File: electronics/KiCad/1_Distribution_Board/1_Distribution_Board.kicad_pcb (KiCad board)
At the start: 2 copper layers, 130 x 120 mm, 135 parts, among them J1 Jumper Pins, J10 Conn_01x08_Socket, J11 Conn_01x08_Socket, J12 Conn_01x02, J13 Conn_01x02, J14 Conn_01x08_Socket, J15 Conn_01x08_Socket, J16 JST VH, J17 JST VH, J18 JST VH, J2 Jumper Pins, J20 Conn_01x04, J24 Generic 2.54mm, J25 Generic 2.54mm, J26 Generic 2.54mm, J27 Generic 2.54mm, J28 Generic 2.54mm, J29 Generic 2.54mm, J3 JST PH, J32 Jumper Pins, J33 Jumper Pins, J34 JST PH, J35 Generic 2.54mm, J36 Conn_01x08_Socket, J37 Conn_01x02_Socket, J38 Conn_01x08_Socket, J39 Jumper Pins, J4 Generic 2.54mm, J40 Jumper Pins, J41 JST PH, J42 Generic 2.54mm, J43 Conn_01x08_Socket, J44 Conn_01x02_Socket, J45 Conn_01x08_Socket, J46 Jumper Pins, J47 Jumper Pins, J48 JST PH, J49 Generic 2.54mm, J5 Conn_01x08_Socket, J50 Conn_01x08_Socket, J51 Conn_01x02_Socket, J52 Conn_01x08_Socket, J53 Conn_01x10, J54 Conn_01x06, J55 Signals 0-3, J56 Signals 4-7, J57 Module Left, J58 Conn_02x08_Odd_Even, J59 Module Right, J6 Conn_01x02_Socket, J60 Signals 8-11, J61 Signals 12-15, J7 Conn_01x08_Socket, J8 Conn_01x02, J9 Conn_01x02, M1 MountingHole_3.2mm_M3_ISO7380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, Q1 DMG2305UX, Q2 BS170, Q3 BS170, SW1 SW_Push, U1 R-786.5-0.5, U2 R-78B12-2.0, U3 R-78C5.0-1.0

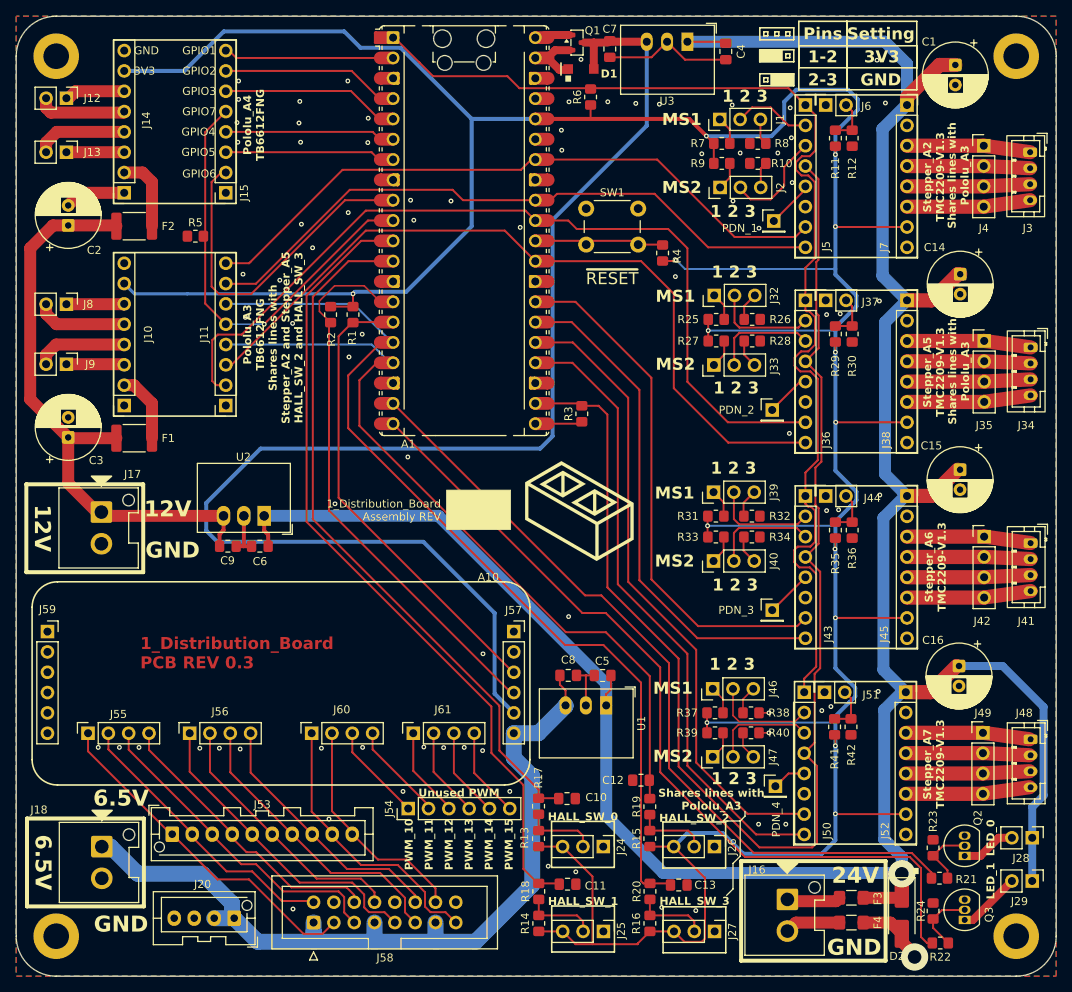
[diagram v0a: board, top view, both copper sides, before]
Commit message: Merge board v1.3 into main (clean-clone fixups, generated files trimmed to main level) (#289)
* Initial start to updates

Removed motor pages, updated Q2,Q3, Cleaned up power module connections.

- Still need to correct routing for these updates.

* PCA Update

Updated PCA to have level shifter for I2C lines and external oscillator for precision. Corrected Power to pull from 12V.

* Removed old circuits from PCB

Removed all unused traces

* Mid work update

Lots of rework on the SCH and PCB. Checkpoint.

* Updated with more layout

Compelted PCA on board.

* adding libraries

* REV0.9 for review

Took care of all open items on the electronics PCB except for the driver resistor addresses.

* Updates Just prior to Ordering V1.0 PCBs

Updates Just prior to Ordering V1.0 PCBs

* Updates to push to V1.0

Updates to push to V1.0

* Updates to push to V1.0 missing saves. . .

Updates to push to V1.0 missing saves. . .

* Correcting Part rotation for JLCPCB

Several parts needed the "FT Rotation Offset" parameter added to correct for part orientation for JLCPCB order.

* All orientations corrected

* latest update

* Updated to reflect V1.0 of layer board as well

Updated for initial orders with PCA module populated. Also updated to layer boards for flex cables.

* Updated data and notes

* Corrected SCH for power sequence issue

5V to Vsys for all powered items.
Correction of the PCA9306 power pins.
Added decoupling to oscillator and PCA9306.

* Updated for changes to the SCH items

Updated PCB to include all changed from the SCH.

* Updated rules to correct errors

Cleaned up rules a bit to prevent false errors.

* Started work on silk update

Slowly started work on silk update.

* Corrected the 10k to 1k for connecting resistors

R1 got fixed for the correct 1k instead of 10k for UART1

* Updated Silk on PCB

Added notes for describing the pins better in the silk layer.

* Updated REV to 1.3 to reflect changes

* Updated with Version 1.3

* KiCad: make the v1.3 project 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
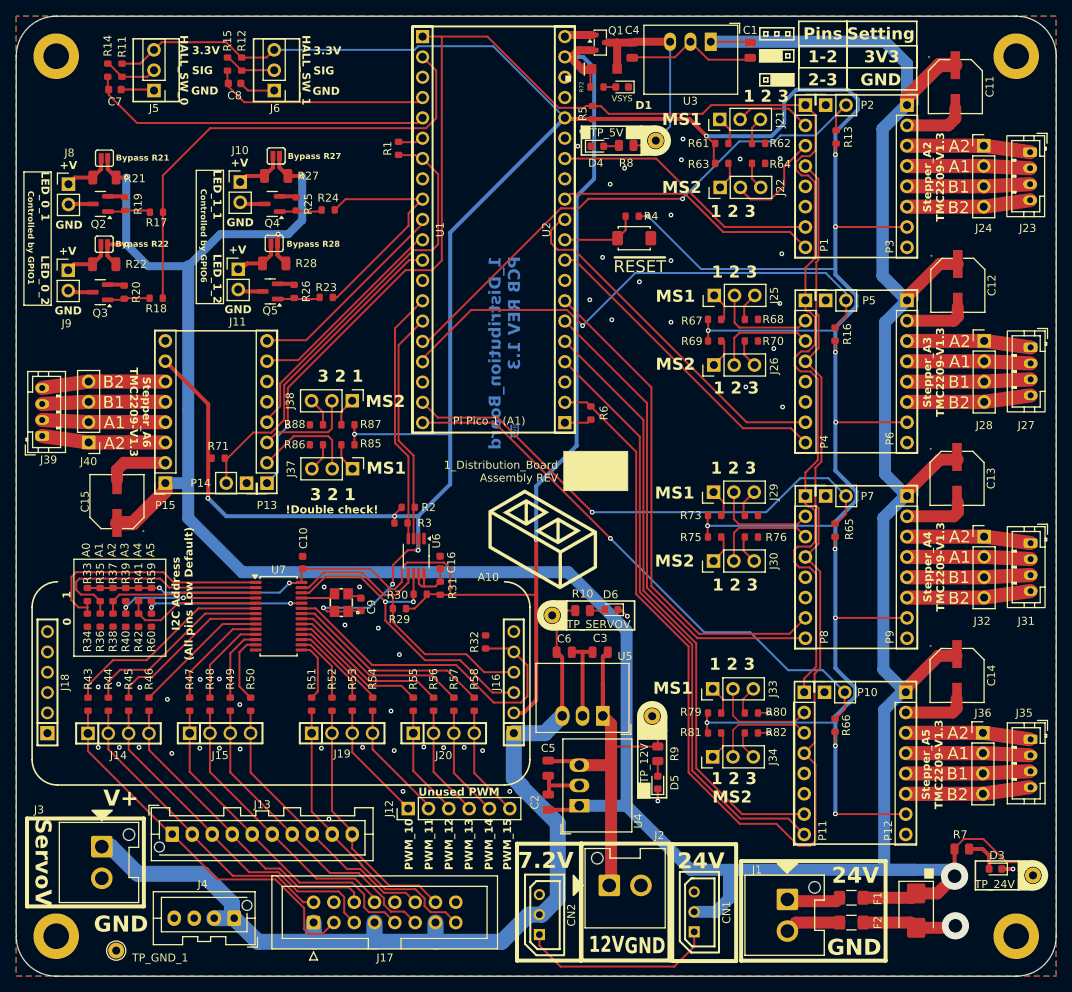
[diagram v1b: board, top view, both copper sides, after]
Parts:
- removed A1: Raspberry Pi Pico 1, Module:RaspberryPi_Pico_Common_Unspecified
- removed the C11 at (93.9, 133.5)
- removed the C12 at (103.1, 120.5)
- removed the C13 at (107.8, 133.6)
- removed the F1 at (39.8, 77.8)
- removed the F2 at (39.8, 51.2)
- removed the J12 at (31.3, 35.2)
- removed the J13 at (31.3, 42.0)
- removed the J26 at (112.3, 128.8)
- removed the J27 at (112.3, 139.4)
- removed the J36 at (123.7, 60.5)
- removed J43, J45, J50, J52, J7: Conn_01x08_Socket, Connector_PinSocket_2.54mm:PinSocket_1x08_P2.54mm_Vertical
- removed J44, J51: Conn_01x02_Socket, Connector_PinSocket_2.54mm:PinSocket_1x02_P2.54mm_Vertical
- removed the J5 at (123.7, 36.1)
- removed J55: Signals 0-3, Connector_PinSocket_2.54mm:PinSocket_1x04_P2.54mm_Vertical
- removed J56: Signals 4-7, Connector_PinSocket_2.54mm:PinSocket_1x04_P2.54mm_Vertical
- removed J57: Module Left, Connector_PinSocket_2.54mm:PinSocket_1x06_P2.54mm_Vertical
- removed J59: Module Right, Connector_PinSocket_2.54mm:PinSocket_1x06_P2.54mm_Vertical
- removed the J6 at (126.2, 36.1)
- removed J60: Signals 8-11, Connector_PinSocket_2.54mm:PinSocket_1x04_P2.54mm_Vertical
- removed J61: Signals 12-15, Connector_PinSocket_2.54mm:PinSocket_1x04_P2.54mm_Vertical
- removed the J8 at (31.3, 61.0)
- removed the J9 at (31.3, 68.5)
- removed PDN_1, PDN_2, PDN_3, PDN_4: PTH, Connector_PinHeader_2.54mm:PinHeader_1x01_P2.54mm_Vertical
- removed SW1: SW_Push, Button_Switch_THT:SW_PUSH_6mm
- added C1: 10uF, PCM_JLCPCB:C_0805, F.Cu at (116.8, 29.2)
- added C15: 100uF, EasyEDA:CAP-SMD_BD6.3-L6.6-W6.6-LS7.4-FD, F.Cu at (37.6, 85.7)
- added C16: 100nF, PCM_JLCPCB:C_0603, F.Cu at (78.0, 93.3)
- added CN1: HC-5264-3A, EasyEDA:CONN-TH_3P-P2.50_HCTL_HC-5264-3A, F.Cu at (109.8, 137.0)
- added CN2: HC-5264-3A, EasyEDA:CONN-TH_3P-P2.50_HCTL_HC-5264-3A, F.Cu at (90.4, 137.3)
- added D3: Yellow, PCM_JLCPCB:D_0603, F.Cu at (147.4, 131.6)
- added D4: Yellow, PCM_JLCPCB:D_0603, F.Cu at (97.7, 41.2)
- added D5: Yellow, PCM_JLCPCB:D_0603, F.Cu at (105.2, 120.8)
- added D6: Yellow, PCM_JLCPCB:D_0603, F.Cu at (99.4, 99.2)
- added D7: Yellow, PCM_JLCPCB:D_0603, F.Cu at (100.7, 33.8)
- added J16: PM254V-11-06-H85, EasyEDA:HDR-TH_6P-P2.54-V-F, F.Cu at (87.2, 108.3)
- added J18: PM254V-11-06-H85, EasyEDA:HDR-TH_6P-P2.54-V-F, F.Cu at (28.9, 108.3)
- added J19: 2.54-1*4P母, EasyEDA:HDR-TH_4P-P2.54-V-F, F.Cu at (65.7, 114.6)
- added J20: 2.54-1*4P母, EasyEDA:HDR-TH_4P-P2.54-V-F, F.Cu at (78.4, 114.6)
- added J39: JST PH, Connector_JST:JST_PH_B4B-PH-K_1x04_P2.00mm_Vertical, F.Cu at (28.3, 77.5)
- added J40: Generic 2.54mm, Connector_PinHeader_2.54mm:PinHeader_1x04_P2.54mm_Vertical, F.Cu at (34.1, 78.3)
- added JAW: Maker's Mark, JAW:JAW, B.Cu at (87.4, 76.8)
- added JP1: ~, PCM_SparkFun-Jumper:Jumper_2_NO, F.Cu at (36.0, 42.8)
- added JP2: ~, PCM_SparkFun-Jumper:Jumper_2_NO, F.Cu at (36.0, 53.5)
- added JP3: ~, PCM_SparkFun-Jumper:Jumper_2_NO, F.Cu at (57.5, 42.5)
- added JP4: ~, PCM_SparkFun-Jumper:Jumper_2_NO, F.Cu at (57.2, 53.4)
- added P1: Header-Female-2.54_1x8, Connector_PinSocket_2.54mm:PinSocket_1x08_P2.54mm_Vertical, F.Cu at (123.7, 36.1)
- added P10: Header-Female-2.54_1x8, Connector_PinSocket_2.54mm:PinSocket_1x08_P2.54mm_Vertical, F.Cu at (123.5, 109.5)
- added P11: Header-Female-2.54_1x2, Connector_PinSocket_2.54mm:PinSocket_1x02_P2.54mm_Vertical, F.Cu at (126.0, 109.5)
- added P12: Header-Female-2.54_1x8, Connector_PinSocket_2.54mm:PinSocket_1x08_P2.54mm_Vertical, F.Cu at (136.2, 109.5)
- added P13: Header-Female-2.54_1x8, Connector_PinSocket_2.54mm:PinSocket_1x08_P2.54mm_Vertical, F.Cu at (56.3, 83.4)
- added P14: Header-Female-2.54_1x2, Connector_PinSocket_2.54mm:PinSocket_1x02_P2.54mm_Vertical, F.Cu at (53.8, 83.4)
- added P15: Header-Female-2.54_1x8, Connector_PinSocket_2.54mm:PinSocket_1x08_P2.54mm_Vertical, F.Cu at (43.6, 83.4)
- added P2: Header-Female-2.54_1x2, Connector_PinSocket_2.54mm:PinSocket_1x02_P2.54mm_Vertical, F.Cu at (126.2, 36.1)
- added P3: Header-Female-2.54_1x8, Connector_PinSocket_2.54mm:PinSocket_1x08_P2.54mm_Vertical, F.Cu at (136.3, 36.1)
- added P4: Header-Female-2.54_1x8, Connector_PinSocket_2.54mm:PinSocket_1x08_P2.54mm_Vertical, F.Cu at (123.7, 60.5)
- added P5: Header-Female-2.54_1x2, Connector_PinSocket_2.54mm:PinSocket_1x02_P2.54mm_Vertical, F.Cu at (126.2, 60.5)
- added P6: Header-Female-2.54_1x8, Connector_PinSocket_2.54mm:PinSocket_1x08_P2.54mm_Vertical, F.Cu at (136.3, 60.5)
- added P7: Header-Female-2.54_1x8, Connector_PinSocket_2.54mm:PinSocket_1x08_P2.54mm_Vertical, F.Cu at (123.7, 85.0)
- added P8: Header-Female-2.54_1x2, Connector_PinSocket_2.54mm:PinSocket_1x02_P2.54mm_Vertical, F.Cu at (126.2, 85.0)
- added P9: Header-Female-2.54_1x8, Connector_PinSocket_2.54mm:PinSocket_1x08_P2.54mm_Vertical, F.Cu at (136.3, 85.0)
- added Q4: AO3400A, PCM_JLCPCB:Q_SOT-23, F.Cu at (57.0, 48.5)
- added Q5: AO3400A, PCM_JLCPCB:Q_SOT-23, F.Cu at (56.8, 59.4)
- added R43: 220Ω, PCM_JLCPCB:R_0603, F.Cu at (34.0, 111.0)
- added R44: 220Ω, PCM_JLCPCB:R_0603, F.Cu at (36.5, 111.0)
- added R45: 220Ω, PCM_JLCPCB:R_0603, F.Cu at (39.1, 111.0)
- added R46: 220Ω, PCM_JLCPCB:R_0603, F.Cu at (41.6, 111.0)
- added R47: 220Ω, PCM_JLCPCB:R_0603, F.Cu at (46.7, 111.0)
- added R48: 220Ω, PCM_JLCPCB:R_0603, F.Cu at (49.2, 111.0)
- added R49: 220Ω, PCM_JLCPCB:R_0603, F.Cu at (51.8, 111.0)
- added R50: 220Ω, PCM_JLCPCB:R_0603, F.Cu at (54.3, 111.0)
- added R51: 220Ω, PCM_JLCPCB:R_0603, F.Cu at (61.9, 111.0)
- added R52: 220Ω, PCM_JLCPCB:R_0603, F.Cu at (64.5, 111.0)
- added R53: 220Ω, PCM_JLCPCB:R_0603, F.Cu at (67.0, 111.0)
- added R54: 220Ω, PCM_JLCPCB:R_0603, F.Cu at (69.6, 111.0)
- added R55: 220Ω, PCM_JLCPCB:R_0603, F.Cu at (74.6, 111.0)
- added R56: 220Ω, PCM_JLCPCB:R_0603, F.Cu at (77.2, 111.0)
- added R57: 220Ω, PCM_JLCPCB:R_0603, F.Cu at (79.7, 111.0)
- added R58: 220Ω, PCM_JLCPCB:R_0603, F.Cu at (82.3, 111.0)
- added R59: 10kΩ, PCM_JLCPCB:R_0603, F.Cu at (41.9, 97.3)
- added R60: 10kΩ, PCM_JLCPCB:R_0603, F.Cu at (41.9, 100.5)
- added R61: 10kΩ, PCM_JLCPCB:R_0603, F.Cu at (113.2, 40.9)
- added R62: 10kΩ, PCM_JLCPCB:R_0603, F.Cu at (117.8, 40.9)
- added R63: 10kΩ, PCM_JLCPCB:R_0603, F.Cu at (113.2, 43.4)
- added R64: 10kΩ, PCM_JLCPCB:R_0603, F.Cu at (117.8, 43.4)
- added R65: 10kΩ, PCM_JLCPCB:R_0603, F.Cu at (127.4, 89.2)
- added R66: 10kΩ, PCM_JLCPCB:R_0603, F.Cu at (127.4, 113.6)
- added R67: 10kΩ, PCM_JLCPCB:R_0603, F.Cu at (112.3, 62.9)
- added R68: 10kΩ, PCM_JLCPCB:R_0603, F.Cu at (116.9, 62.9)
- added R69: 10kΩ, PCM_JLCPCB:R_0603, F.Cu at (112.3, 65.6)
- added R70: 10kΩ, PCM_JLCPCB:R_0603, F.Cu at (116.9, 65.6)
- added R71: 10kΩ, PCM_JLCPCB:R_0603, F.Cu at (50.2, 80.2)
- added R72: 300Ω, PCM_JLCPCB:R_0603, F.Cu at (97.6, 33.8)
- added R73: 10kΩ, PCM_JLCPCB:R_0603, F.Cu at (112.3, 87.4)
- added R74: 10kΩ, PCM_JLCPCB:R_0603, F.Cu at (116.9, 87.4)
- added R75: 10kΩ, PCM_JLCPCB:R_0603, F.Cu at (112.3, 90.1)
- added R76: 10kΩ, PCM_JLCPCB:R_0603, F.Cu at (116.9, 90.1)
- added R79: 10kΩ, PCM_JLCPCB:R_0603, F.Cu at (112.3, 112.1)
- added R80: 10kΩ, PCM_JLCPCB:R_0603, F.Cu at (116.9, 112.1)
- added R81: 10kΩ, PCM_JLCPCB:R_0603, F.Cu at (112.3, 114.6)
- added R82: 10kΩ, PCM_JLCPCB:R_0603, F.Cu at (116.9, 114.6)
- added R85: 10kΩ, PCM_JLCPCB:R_0603, F.Cu at (66.5, 78.6)
- added R86: 10kΩ, PCM_JLCPCB:R_0603, F.Cu at (62.5, 78.6)
- added R87: 10kΩ, PCM_JLCPCB:R_0603, F.Cu at (66.5, 76.1)
- added R88: 10kΩ, PCM_JLCPCB:R_0603, F.Cu at (62.5, 76.1)
- added S1: Tactile Button, 160gf, PCM_JLCPCB:SW_TS-1088-AR02016, F.Cu at (102.2, 52.8)
- added TP_12V_1: PTH, TestPoint:TestPoint_THTPad_D2.0mm_Drill1.0mm, F.Cu at (104.5, 112.5)
- added TP_24V_1: PTH, TestPoint:TestPoint_THTPad_D2.0mm_Drill1.0mm, F.Cu at (152.1, 132.4)
- added TP_5V_1: PTH, TestPoint:TestPoint_THTPad_D2.0mm_Drill1.0mm, F.Cu at (105.0, 40.5)
- added TP_GND_1: PTH, TestPoint:TestPoint_THTPad_D2.0mm_Drill1.0mm, F.Cu at (37.5, 141.8)
- added TP_ServoV_1: PTH, TestPoint:TestPoint_THTPad_D2.0mm_Drill1.0mm, F.Cu at (92.0, 99.9)
- added U2: KH-2.54FH-1X20P-H8.5, EasyEDA:HDR-TH_20P-P2.54-V-F-2, F.Cu at (93.6, 51.7)
- added U5: R-78B6.5-1.5, Converter_DCDC:Converter_DCDC_RECOM_R-78B-2.0_THT, F.Cu at (98.3, 112.5)
- added U6: PCA9306, Package_SO:Texas_S-PDSO-G8_3x3mm_P0.65mm, F.Cu at (75.0, 92.5)
- added U7: PCA9685PW, Package_SO:TSSOP-28_4.4x9.7mm_P0.65mm, F.Cu at (57.8, 100.0)
- added Y1: 25MHz, PCM_SparkFun-Clock:Crystal_SMD_3.2x2.5mm, F.Cu at (65.6, 98.3)
- C10: value 0.1uf -> 10uF; footprint Capacitor_SMD:C_0805_2012Metric_Pad1.18x1.45mm_HandSolder -> PCM_JLCPCB:C_0603
- C11: renamed from C1; footprint Capacitor_THT:CP_Radial_D8.0mm_P2.50mm -> EasyEDA:CAP-SMD_BD6.3-L6.6-W6.6-LS7.4-FD
- C12: renamed from C14; footprint Capacitor_THT:CP_Radial_D8.0mm_P2.50mm -> EasyEDA:CAP-SMD_BD6.3-L6.6-W6.6-LS7.4-FD
- C13: renamed from C15; footprint Capacitor_THT:CP_Radial_D8.0mm_P2.50mm -> EasyEDA:CAP-SMD_BD6.3-L6.6-W6.6-LS7.4-FD
- C14: renamed from C16; footprint Capacitor_THT:CP_Radial_D8.0mm_P2.50mm -> EasyEDA:CAP-SMD_BD6.3-L6.6-W6.6-LS7.4-FD
- C2, C3: value 100uF -> 10uF; footprint Capacitor_THT:CP_Radial_D8.0mm_P2.50mm -> PCM_JLCPCB:C_0805
- C4, C5, C6: value 10uf -> 10uF; footprint Capacitor_SMD:C_0805_2012Metric_Pad1.18x1.45mm_HandSolder -> PCM_JLCPCB:C_0805
- C7, C8, C9: value 10uf -> 100nF; footprint Capacitor_SMD:C_0805_2012Metric_Pad1.18x1.45mm_HandSolder -> PCM_JLCPCB:C_0603
- D2: value TBD -> SK84B; footprint Diode_SMD:D_SMA_Handsoldering -> PCM_JLCPCB:D_SMB
- J10, J11: value Conn_01x08_Socket -> Generic 2.54mm; footprint Connector_PinSocket_2.54mm:PinSocket_1x08_P2.54mm_Vertical -> Connector_PinHeader_2.54mm:PinHeader_1x02_P2.54mm_Vertical
- J14, J15: value Conn_01x08_Socket -> 2.54-1*4P母; footprint Connector_PinSocket_2.54mm:PinSocket_1x08_P2.54mm_Vertical -> EasyEDA:HDR-TH_4P-P2.54-V-F
- J37: value Conn_01x02_Socket -> Jumper Pins; footprint Connector_PinSocket_2.54mm:PinSocket_1x02_P2.54mm_Vertical -> Connector_PinHeader_2.54mm:PinHeader_1x03_P2.54mm_Vertical
- J38: value Conn_01x08_Socket -> Jumper Pins; footprint Connector_PinSocket_2.54mm:PinSocket_1x08_P2.54mm_Vertical -> Connector_PinHeader_2.54mm:PinHeader_1x03_P2.54mm_Vertical
- Q2, Q3: value BS170 -> AO3400A; footprint Package_TO_SOT_THT:TO-92_Inline -> PCM_JLCPCB:Q_SOT-23
- R1, R23, R24, R6: value 10k -> 1kΩ; footprint Resistor_SMD:R_0805_2012Metric_Pad1.20x1.40mm_HandSolder -> PCM_JLCPCB:R_0603
- R10, R8: value 10k -> 1kΩ; footprint Resistor_SMD:R_0805_2012Metric_Pad1.20x1.40mm_HandSolder -> PCM_JLCPCB:R_0805
- R11, R12, R2, R25, R26, R29, R30, R32, R33, R34, R35, R36, R37, R38, R39, R4, R40, R41, R42, R5: value 10k -> 10kΩ; footprint Resistor_SMD:R_0805_2012Metric_Pad1.20x1.40mm_HandSolder -> PCM_JLCPCB:R_0603
- R13, R16: value 10K -> 10kΩ; footprint Resistor_SMD:R_0805_2012Metric_Pad1.20x1.40mm_HandSolder -> PCM_JLCPCB:R_0603
- R14, R15: value 10K -> 100Ω; footprint Resistor_SMD:R_0805_2012Metric_Pad1.20x1.40mm_HandSolder -> PCM_JLCPCB:R_0603
- R17, R18: value 100 -> 1kΩ; footprint Resistor_SMD:R_0805_2012Metric_Pad1.20x1.40mm_HandSolder -> PCM_JLCPCB:R_0603
- R19, R20: value 100 -> 10kΩ; footprint Resistor_SMD:R_0805_2012Metric_Pad1.20x1.40mm_HandSolder -> PCM_JLCPCB:R_0603
- R21, R22: value 150 -> 180Ω; footprint Resistor_SMD:R_0805_2012Metric_Pad1.20x1.40mm_HandSolder -> PCM_JLCPCB:R_1206
- R27, R28: value 10k -> 180Ω; footprint Resistor_SMD:R_0805_2012Metric_Pad1.20x1.40mm_HandSolder -> PCM_JLCPCB:R_1206
- R3: value 1k -> 10kΩ; footprint Resistor_SMD:R_0805_2012Metric_Pad1.20x1.40mm_HandSolder -> PCM_JLCPCB:R_0603
- R31: value 10k -> 200kΩ; footprint Resistor_SMD:R_0805_2012Metric_Pad1.20x1.40mm_HandSolder -> PCM_JLCPCB:R_0603
- R7: value 10k -> 5.1kΩ; footprint Resistor_SMD:R_0805_2012Metric_Pad1.20x1.40mm_HandSolder -> PCM_JLCPCB:R_0805
- R9: value 10k -> 2.2kΩ; footprint Resistor_SMD:R_0805_2012Metric_Pad1.20x1.40mm_HandSolder -> PCM_JLCPCB:R_0805
- U1: value R-786.5-0.5 -> KH-2.54FH-1X20P-H8.5; footprint Converter_DCDC:Converter_DCDC_RECOM_R-78E-0.5_THT -> EasyEDA:HDR-TH_20P-P2.54-V-F-2
- moved J8 145.6 mm to (31.5, 46.0), turned to 0 degrees
- moved J9 142.6 mm to (31.5, 56.8), turned to 0 degrees
- moved R21 136.3 mm to (36.0, 45.2), turned to 180 degrees
- moved Q2 135.3 mm to (35.5, 48.5), turned to 180 degrees
- moved R22 134.6 mm to (36.0, 56.0), turned to 180 degrees
- moved Q3 133.5 mm to (35.5, 59.5), turned to 180 degrees
- moved R14 119.5 mm to (36.4, 31.8), turned to -90 degrees
- moved R24 115.7 mm to (64.0, 49.2), turned to 180 degrees
- moved J6 112.9 mm to (57.2, 34.3), turned to 180 degrees
- moved R15 110.3 mm to (51.4, 31.0), turned to -90 degrees
- moved J5 109.9 mm to (42.2, 34.3), turned to 180 degrees
- moved R23 102.4 mm to (63.8, 60.1), turned to 180 degrees
- moved R19 99.9 mm to (38.6, 48.5)
- moved R20 99.6 mm to (38.5, 59.5)
- moved R13 95.3 mm to (127.5, 40.1)
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- renumbered F3 to F1, F4 to F2, J16 to J1, J54 to J12, J53 to J13, J58 to J17, J17 to J2, J1 to J21, J2 to J22, J3 to J23, J4 to J24, J32 to J25, J33 to J26, J34 to J27, J35 to J28, J39 to J29, J18 to J3, J40 to J30, J41 to J31, J42 to J32, J46 to J33, J47 to J34, J48 to J35, J49 to J36, J20 to J4, J24 to J5, J25 to J6, J28 to J8, J29 to J9, U2 to U4
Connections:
- net /Stepper Module/A1 renamed /Stepper Module/A_1
- net /Stepper Module/A2 renamed /Stepper Module/A_2
- net /Stepper Module/B1 renamed /Stepper Module/B_1
- net /Stepper Module/B2 renamed /Stepper Module/B_2
- net /Stepper Module2/A1 renamed /Stepper Module2/A_1
- net /Stepper Module2/A2 renamed /Stepper Module2/A_2
- net /Stepper Module2/B1 renamed /Stepper Module2/B_1
- net /Stepper Module2/B2 renamed /Stepper Module2/B_2
- net /Stepper Module2/DIAG renamed /PCA9685 Module/A1
- net /Stepper Module3/A1 renamed /Stepper Module3/A_1
- net /Stepper Module3/A2 renamed /Stepper Module3/A_2
- net /Stepper Module3/B1 renamed /Stepper Module3/B_1
- net /Stepper Module3/B2 renamed /Stepper Module3/B_2
- net /Stepper Module3/DIAG renamed /PCA9685 Module/A4
- C10 pad 1: /GPIO9-GPIO_IN_HALL-SW_0 -> VSYS
- C2 pad 1: +12V -> +24V
- C4 pad 1: +24V -> +5V
- C5 pad 1: +24V -> +12V
- C6 pad 1: +24V -> +ServoV
- C7 pad 1: +5V -> /GPIO3-GPIO_IN_HALL-SW_0
- C8 pad 1: +6.5V -> /GPIO2-GPIO_IN_HALL-SW_1
- C9 pad 1: +12V -> GND
- C9 pad 2: GND -> +3V3
- D1 pad 1: /VSYS -> VSYS
- J10 pad 1: GND -> Net-(J10-Pin_1)
- J10 pad 2: /DC Motor Control_0/VMOT -> Net-(J10-Pin_2)
- J11 pad 1: GND -> Net-(J11-Pin_1)
- J11 pad 2: /GPIO26-PWM5_A-Stepper1_STEP -> Net-(J11-Pin_2)
- J14 pad 1: GND -> /PCA9685 Module/PWM_0
- J14 pad 2: /DC Motor Control_1/VMOT -> /PCA9685 Module/PWM_1
- J14 pad 3: /DC Motor Control_1/BO_1 -> /PCA9685 Module/PWM_2
- J14 pad 4: /DC Motor Control_1/BO_2 -> /PCA9685 Module/PWM_3
- J15 pad 1: GND -> /PCA9685 Module/PWM_4
- J15 pad 2: /GPIO6-PWM3_A-MOTOR1_B_PWM -> /PCA9685 Module/PWM_5
- J15 pad 3: /GPIO5-GPIO_OUT-MOTOR1_B_IN2 -> /PCA9685 Module/PWM_6
- J15 pad 4: /GPIO4-GPIO_OUT-MOTOR1_B_IN1 -> /PCA9685 Module/PWM_7
- J17 pad 1: +6.5V -> +ServoV
- J17 pad 13: +6.5V -> +ServoV
- J17 pad 7: +6.5V -> +ServoV
- J21 pad 1: Net-(J1-Pin_1) (its old number) -> Net-(J21-Pin_1)
- J21 pad 3: Net-(J1-Pin_3) -> Net-(J21-Pin_3)
- J22 pad 1: Net-(J2-Pin_1) -> Net-(J22-Pin_1)
- J22 pad 3: Net-(J2-Pin_3) -> Net-(J22-Pin_3)
- J25 pad 1: Net-(J32-Pin_1) -> Net-(J25-Pin_1)
- J25 pad 3: Net-(J32-Pin_3) -> Net-(J25-Pin_3)
- J26 pad 1: Net-(J33-Pin_1) -> Net-(J26-Pin_1)
- J26 pad 3: Net-(J33-Pin_3) -> Net-(J26-Pin_3)
- J27 pad 1: /Stepper Module1/A2 -> /Stepper Module1/A_2
- J27 pad 2: /Stepper Module1/A1 -> /Stepper Module1/A_1
- J27 pad 3: /Stepper Module1/B1 -> /Stepper Module1/B_1
- J27 pad 4: /Stepper Module1/B2 -> /Stepper Module1/B_2
- J28 pad 1: /Stepper Module1/A2 -> /Stepper Module1/A_2
- J28 pad 2: /Stepper Module1/A1 -> /Stepper Module1/A_1
- J28 pad 3: /Stepper Module1/B1 -> /Stepper Module1/B_1
- J28 pad 4: /Stepper Module1/B2 -> /Stepper Module1/B_2
- J29 pad 1: Net-(J39-Pin_1) -> Net-(J29-Pin_1)
- J29 pad 3: Net-(J39-Pin_3) -> Net-(J29-Pin_3)
- J3 pad 1: +6.5V -> +ServoV
- J30 pad 1: Net-(J40-Pin_1) -> Net-(J30-Pin_1)
- J30 pad 3: Net-(J40-Pin_3) -> Net-(J30-Pin_3)
- J33 pad 1: Net-(J46-Pin_1) -> Net-(J33-Pin_1)
- J33 pad 3: Net-(J46-Pin_3) -> Net-(J33-Pin_3)
- J34 pad 1: Net-(J47-Pin_1) -> Net-(J34-Pin_1)
- J34 pad 3: Net-(J47-Pin_3) -> Net-(J34-Pin_3)
- J37 pad 1: /Stepper Module1/VREF -> Net-(J37-Pin_1)
- J37 pad 2: /Stepper Module1/DIAG -> /Stepper Module4/MS1
- J38 pad 1: +24V -> Net-(J38-Pin_1)
- J38 pad 2: GND -> /Stepper Module4/MS2
- J38 pad 3: /Stepper Module1/A2 -> Net-(J38-Pin_3)
- J4 pad 1: +6.5V -> +ServoV
- J4 pad 2: +6.5V -> +ServoV
- J5 pad 2: Net-(J24-Pin_2) -> Net-(J5-Pin_2)
- J6 pad 2: Net-(J25-Pin_2) -> Net-(J6-Pin_2)
- J8 pad 1: +24V -> Net-(J8-Pin_1)
- J8 pad 2: Net-(J28-Pin_2) -> Net-(J8-Pin_2)
- J9 pad 1: +24V -> Net-(J9-Pin_1)
- J9 pad 2: Net-(J29-Pin_2) -> Net-(J9-Pin_2)
- Q1 pad 2: /VSYS -> VSYS
- Q2 pad 1: Net-(J28-Pin_2) -> Net-(Q2-G)
- Q2 pad 2: Net-(Q2-G) -> GND
- Q2 pad 3: GND -> Net-(J8-Pin_2)
- Q3 pad 1: Net-(J29-Pin_2) -> Net-(Q3-G)
- Q3 pad 2: Net-(Q3-G) -> GND
- Q3 pad 3: GND -> Net-(J9-Pin_2)
- R1 pad 1: +3V3 -> /GPIO4-UART1_TX
- R1 pad 2: /I2C1_SCL-PCA9685_SCL -> /GPIO5-UART1_RX-StepperUART_1
- R10 pad 1: Net-(J2-Pin_3) -> +ServoV
- R10 pad 2: GND -> Net-(D6-Pad2)
- R11 pad 2: /Stepper Module/DIAG -> Net-(J5-Pin_2)
- R12 pad 1: /Stepper Module/DIAG -> +3V3
- R12 pad 2: GND -> Net-(J6-Pin_2)
- R13 pad 2: Net-(J24-Pin_2) -> /GPIO12-GPIO_IN-Stepper_DIAG
- R14 pad 1: +3V3 -> Net-(J5-Pin_2)
- R14 pad 2: Net-(J25-Pin_2) -> /GPIO3-GPIO_IN_HALL-SW_0
- R15 pad 1: +3V3 -> Net-(J6-Pin_2)
- R15 pad 2: Net-(J26-Pin_2) -> /GPIO2-GPIO_IN_HALL-SW_1
- R16 pad 2: Net-(J27-Pin_2) -> /GPIO13-GPIO_IN-Stepper1_DIAG
- R17 pad 1: Net-(J24-Pin_2) -> /GPIO1-GPIO_OUT-LED_0
- R17 pad 2: /GPIO9-GPIO_IN_HALL-SW_0 -> Net-(Q2-G)
- R18 pad 1: Net-(J25-Pin_2) -> /GPIO1-GPIO_OUT-LED_0
- R18 pad 2: /GPIO8-GPIO_IN_HALL-SW_1 -> Net-(Q3-G)
- R19 pad 1: Net-(J26-Pin_2) -> Net-(Q2-G)
- R19 pad 2: /GPIO13-GPIO_IN_HALL-SW_2 -> GND
- R2 pad 2: /I2C1_SDA-PCA9685_SDA -> /I2C1_SCL-PCA9685_SCL
- R20 pad 1: Net-(J27-Pin_2) -> Net-(Q3-G)
- R20 pad 2: /GPIO12-GPIO_IN_HALL-SW_3 -> GND
- R21 pad 1: /GPIO14-GPIO_OUT-LED_0 -> +24V
- R21 pad 2: Net-(Q2-G) -> Net-(J8-Pin_1)
- R22 pad 1: /GPIO15-GPIO_OUT-LED_1 -> +24V
- R22 pad 2: Net-(Q3-G) -> Net-(J9-Pin_1)
- R23 pad 1: Net-(Q2-G) -> /GPIO6-GPIO_OUT-LED_1
- R23 pad 2: GND -> Net-(Q5-G)
- R24 pad 1: Net-(Q3-G) -> /GPIO6-GPIO_OUT-LED_1
- R24 pad 2: GND -> Net-(Q4-G)
- R25 pad 1: +3V3 -> Net-(Q4-G)
- R25 pad 2: Net-(J32-Pin_1) -> GND
- R26 pad 1: Net-(J32-Pin_3) -> Net-(Q5-G)
- R27 pad 1: +3V3 -> +24V
- R27 pad 2: Net-(J33-Pin_1) -> Net-(J10-Pin_1)
- R28 pad 1: Net-(J33-Pin_3) -> +24V
- R28 pad 2: GND -> Net-(J11-Pin_1)
- R29 pad 1: +3V3 -> VSYS
- R29 pad 2: /Stepper Module1/DIAG -> /PCA9685 Module/I2C0_SDA_5V
- R3 pad 1: /GPIO16-UART0_TX -> +3V3
- R3 pad 2: /GPIO17-UART0_RX-StepperUART -> /I2C1_SDA-PCA9685_SDA
- R30 pad 1: /Stepper Module1/DIAG -> VSYS
- R30 pad 2: GND -> /PCA9685 Module/I2C0_SCL_5V
- R31 pad 1: +3V3 -> VSYS
- R31 pad 2: Net-(J39-Pin_1) -> Net-(U6-EN)
- R32 pad 1: Net-(J39-Pin_3) -> /PCA9685 Module/~{OE}
- R33 pad 1: +3V3 -> VSYS
- R33 pad 2: Net-(J40-Pin_1) -> /PCA9685 Module/A0
- R34 pad 1: Net-(J40-Pin_3) -> /PCA9685 Module/A0
- R35 pad 1: +3V3 -> VSYS
- R37 pad 1: +3V3 -> VSYS
- R37 pad 2: Net-(J46-Pin_1) -> /PCA9685 Module/A2
- R38 pad 1: Net-(J46-Pin_3) -> /PCA9685 Module/A2
- R39 pad 1: +3V3 -> VSYS
- R39 pad 2: Net-(J47-Pin_1) -> /PCA9685 Module/A3
- R40 pad 1: Net-(J47-Pin_3) -> /PCA9685 Module/A3
- R41 pad 1: +3V3 -> VSYS
- R5 pad 1: /GPIO7-GPIO_OUT-Motor_~{STBY} -> +3V3
- R5 pad 2: GND -> /GPIO0-GPIO_OUT-~{EN}_Stepper
- R6 pad 1: +3V3 -> /GPIO16-UART0_TX
- R6 pad 2: /GPIO0-GPIO_OUT-~{EN}_Stepper -> /GPIO17-UART0_RX-StepperUART
- R7 pad 1: +3V3 -> +24V
- R7 pad 2: Net-(J1-Pin_1) (its old number) -> Net-(D3-Pad2)
- R8 pad 1: Net-(J1-Pin_3) -> +5V
- R8 pad 2: GND -> Net-(D4-Pad2)
- R9 pad 1: +3V3 -> +12V
- R9 pad 2: Net-(J2-Pin_1) -> Net-(D5-Pad2)
- U1 pad 1: +24V -> /GPIO0-GPIO_OUT-~{EN}_Stepper
- U1 pad 2: GND -> /GPIO1-GPIO_OUT-LED_0
- U1 pad 3: +6.5V -> GND
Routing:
- net VSYS: track 0.00 -> 170.5 mm, vias 0 -> 3
- net +5V: track 169.4 -> 27.4 mm
- net +ServoV: track 0.00 -> 121.0 mm
- net +24V: track 335.0 -> 451.8 mm, vias 1 -> 5
- net /GPIO12-GPIO_IN_HALL-SW_3: track 114.5 -> 0.00 mm
- net /GPIO15-GPIO_OUT-LED_1: track 107.0 -> 0.00 mm
- net +6.5V: track 104.3 -> 0.00 mm
- net /GPIO8-GPIO_IN_HALL-SW_1: track 101.0 -> 0.00 mm
- net /GPIO14-GPIO_OUT-LED_0: track 100.0 -> 0.00 mm
- net /GPIO13-GPIO_IN_HALL-SW_2: track 96.6 -> 0.00 mm
- net /GPIO9-GPIO_IN_HALL-SW_0: track 88.0 -> 0.00 mm
- net /GPIO15-GPIO_IN-Stepper3_DIAG: track 0.00 -> 70.6 mm, vias 0 -> 1
- net /GPIO12-GPIO_IN-Stepper_DIAG: track 0.00 -> 68.9 mm, vias 0 -> 1
- net /GPIO14-GPIO_IN-Stepper2_DIAG: track 0.00 -> 66.0 mm, vias 0 -> 1
- net /GPIO13-GPIO_IN-Stepper1_DIAG: track 0.00 -> 65.3 mm, vias 0 -> 1
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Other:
- board text added: "!Double check!"
- board text added: "+V"
- board text added: "1_Distribution_Board PCB REV 1.3"
- board text added: "3 2 1"
- board text added: "3.3V"
- board text added: "7.2V"
- board text added: "A0 A1 A2 A3 A4 A5"
- board text added: "A1"
- board text added: "A2"
- board text added: "B1"
- board text added: "B2"
- board text added: "Bypass R21"
- board text added: "Bypass R22"
- board text added: "Bypass R27"
- board text added: "Bypass R28"
- board text added: "Controlled by GPIO1"
- board text added: "Controlled by GPIO6"
- board text added: "I2C Address (All pins Low Default)"
- board text added: "LED_0_1"
- board text added: "LED_0_2"
- board text added: "LED_1_1"
- board text added: "LED_1_2"
- board text added: "Pi Pico 1 (A1)"
- board text added: "SIG"
- board text added: "ServoV"
- board text added: "Stepper_A3 TMC2209-V1.3"
- board text added: "Stepper_A4 TMC2209-V1.3"
- board text added: "TP_12V"
- board text added: "TP_24V"
- board text added: "TP_5V"
- board text added: "TP_SERVOV"
- board text added: "V+"
- board text added: "VSYS"
- board text removed: "1_Distribution_Board PCB REV 0.3"
- board text removed: "6.5V"
- board text removed: "GPIO1"
- board text removed: "GPIO2"
- board text removed: "GPIO3"
- board text removed: "GPIO4"
- board text removed: "GPIO5"
- board text removed: "GPIO6"
- board text removed: "GPIO7"
- board text removed: "HALL_SW_2"
- board text removed: "HALL_SW_3"
- board text removed: "LED_0"
- board text removed: "LED_1"
- board text removed: "Pololu_A3 TB6612FNG"
- board text removed: "Pololu_A4 TB6612FNG"
- board text removed: "Shares lines with Pololu_A3"
- board text removed: "Shares lines with Stepper_A2 and Stepper_A5 HALL_SW_2 and HALL_SW_3"
- board text removed: "Stepper_A7 TMC2209-V1.3"
